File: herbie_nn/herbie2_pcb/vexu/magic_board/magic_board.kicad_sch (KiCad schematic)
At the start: 12 parts, among them J1 4P4C, J2 Conn_ARM_JTAG_SWD_10, U2 ATSAMD21G18A-A, U3 BD33FC0WEFJ, Y1 Crystal

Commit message: updated board
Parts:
- added LED1, LED2, PWR1: LED, LED_SMD:LED_1206_3216Metric, symbol Device:LED
- added R3: 10K, Resistor_SMD:R_1206_3216Metric, symbol Device:R
- added R4, R5, R6: 330, Resistor_SMD:R_1206_3216Metric, symbol Device:R
- added U4: ATSAMD51J19A-A, Package_QFP:TQFP-64_10x10mm_P0.5mm, symbol MCU_Microchip_SAMD:ATSAMD51J19A-A
- C1, C2: value C -> 15pF
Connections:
- net Vcc is gone; now on net +12V: J1.4
- net GND: now also BZ1.2 (-), C1.1, C2.1, D1.3 (common), J2.3 (GND), J2.5 (GND), U2.18 (GND), U2.35 (GND), U2.42 (GND), U2.5 (GNDANA), U3.3 (GND), U3.9 (GND), LED1.1 (K), LED2.1 (K), PWR1.1 (K), R3.2
- net RX_BRAIN: now reaches U1.1 (R)
- net RX_BRAIN: now also U2.10 (PA05)
- net DIR_BRAIN: now reaches U1.2 (RE/)
- net DIR_BRAIN: now also U1.3 (DE)
- net TX_BRAIN: now reaches U1.4 (D)
- net TX_BRAIN: now also U2.9 (PA04)
- net +3.3V: now reaches U1.8 (Vcc)
- net +3.3V: now also J2.1 (VTref), U2.17 (VDDIO), U2.36 (VDDIO), U2.44 (VDDIN), U3.1 (VO), R6.2
- net NRESET: now reaches J2.10 (~{RESET})
- net NRESET: now also U2.40 (~{RESET})
- net SWDIO: now reaches J2.2 (SWDIO/TMS)
- net SWDIO: now also U2.46 (PA31)
- net SWCLK: now reaches J2.4 (SWCLK/TCK)
- net SWCLK: now also U2.45 (PA30)
- net +12V: now reaches U3.5 (EN)
- net +12V: now also U3.8 (VCC), R3.1
- net at U2.37 (PB22): now also R4.2
- net at U2.38 (PB23): now also R5.2
- new net: LED2.2 (A), R5.1
- new net: U4.22 (GND), U4.33 (GND), U4.47 (GND), U4.54 (GND)
- new net: PWR1.2 (A), R6.1
- new net: LED1.2 (A), R4.1
- no-connect marks 0 -> 3
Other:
- moved on the sheet: C1, C2, R1, R2, U1, U3

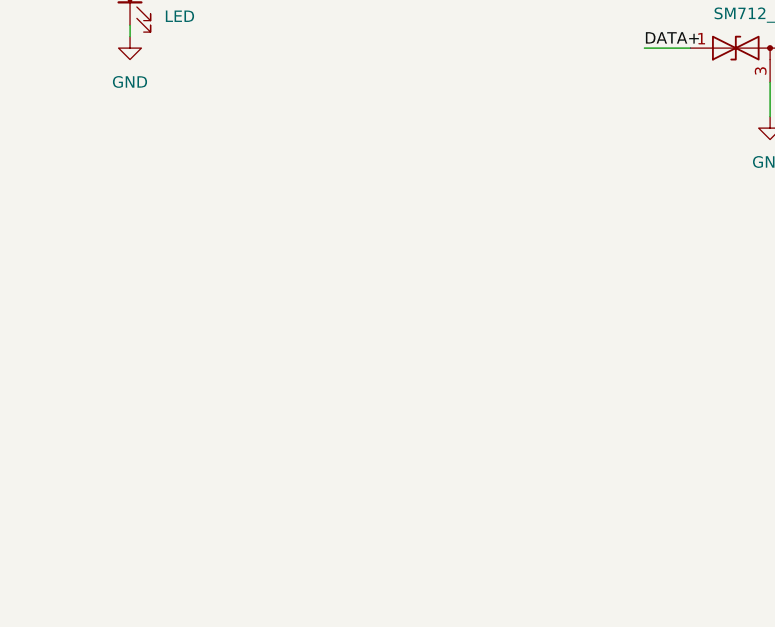
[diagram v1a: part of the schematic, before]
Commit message: added SAMD51 and encoder chips
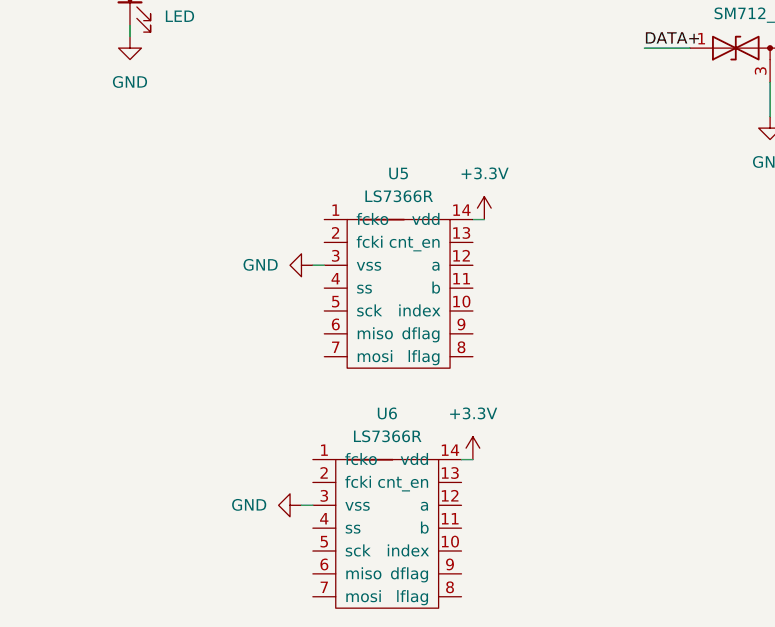
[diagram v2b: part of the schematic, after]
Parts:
- added U5, U6: LS7366R, Package_SO:SOIC-14_3.9x8.7mm_P1.27mm, symbol js:LS7366R
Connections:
- net +3.3V: now also U5.14 (vdd), U6.14 (vdd)
- net GND: now also U5.3 (vss), U6.3 (vss)

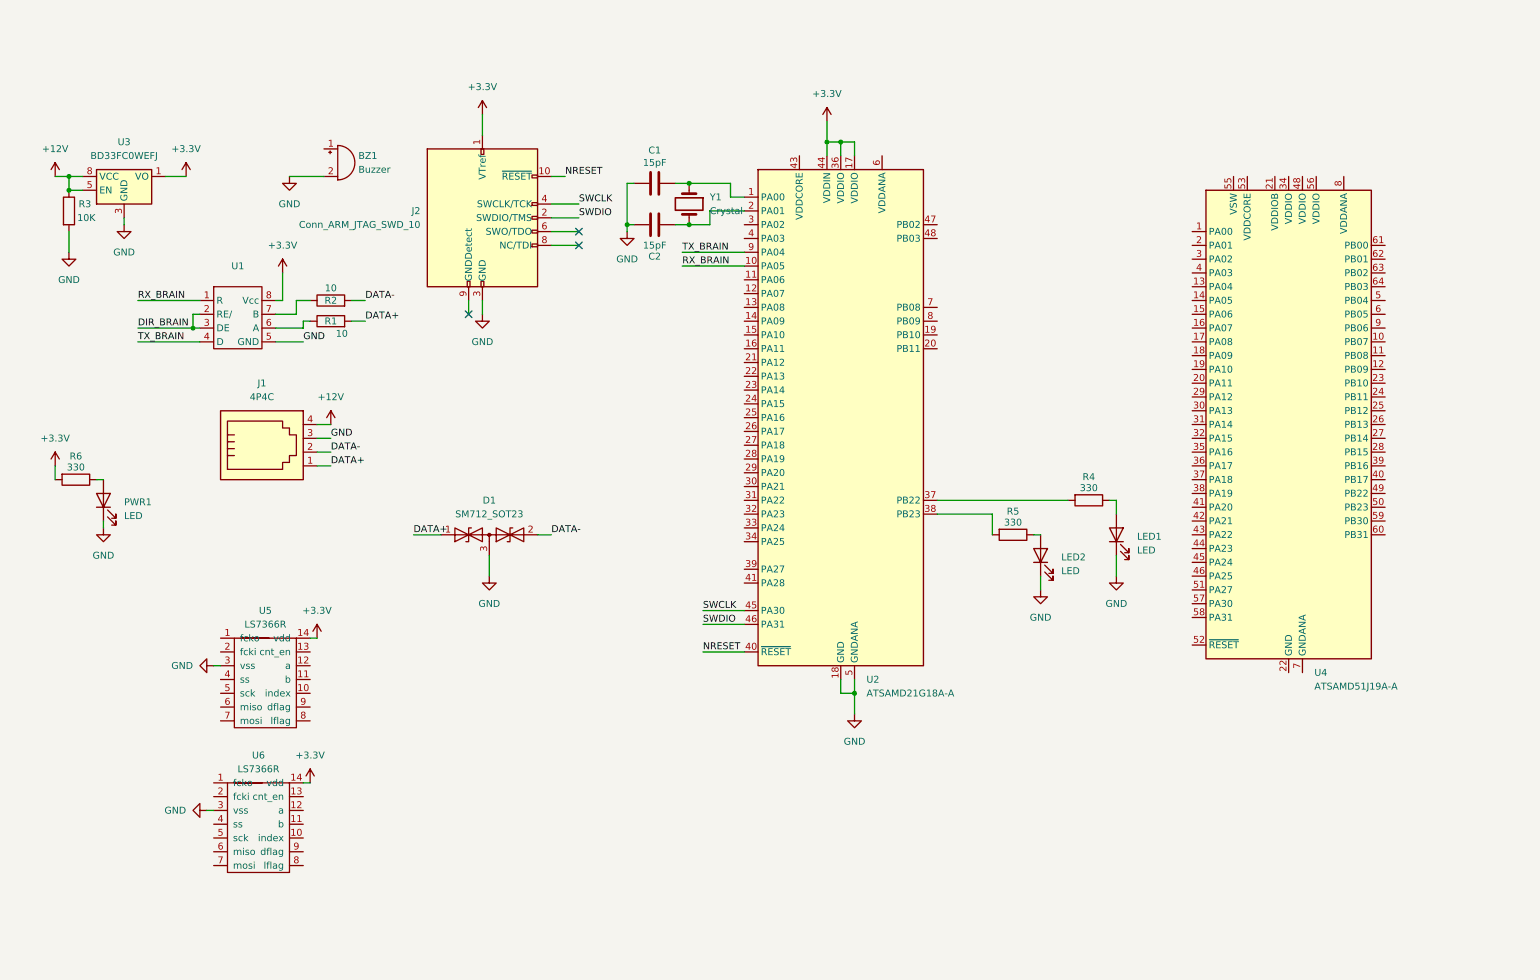
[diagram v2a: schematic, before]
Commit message: changed to SAMD51J19
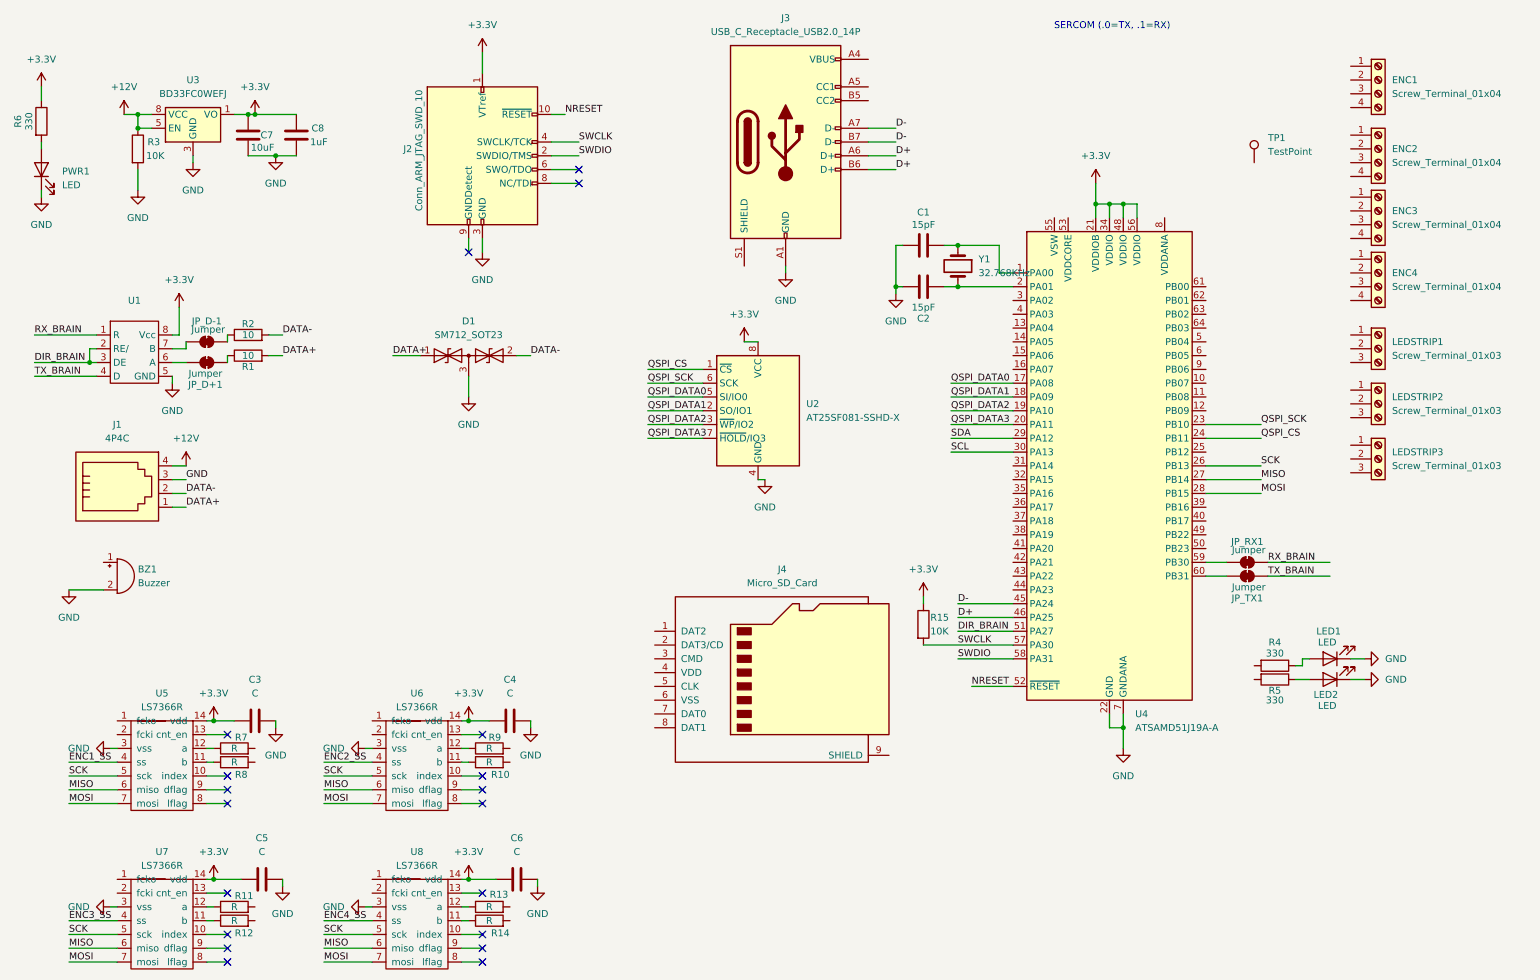
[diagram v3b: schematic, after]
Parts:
- removed U2: ATSAMD21G18A-A, Package_QFP:TQFP-48_7x7mm_P0.5mm, symbol MCU_Microchip_SAMD:ATSAMD21G18A-A
- added C3, C4, C5, C6: C, Capacitor_SMD:C_1206_3216Metric, symbol Device:C
- added C7: 10uF, Capacitor_SMD:C_1206_3216Metric, symbol Device:C
- added C8: 1uF, Capacitor_SMD:C_1206_3216Metric, symbol Device:C
- added ENC1, ENC2, ENC3, ENC4: Screw_Terminal_01x04, TerminalBlock_Phoenix:TerminalBlock_Phoenix_MPT-0,5-4-2.54_1x04_P2.54mm_Horizontal, symbol Connector:Screw_Terminal_01x04
- added J3: USB_C_Receptacle_USB2.0_14P, Connector_USB:USB_C_Receptacle_GCT_USB4085, symbol Connector:USB_C_Receptacle_USB2.0_14P
- added J4: Micro_SD_Card, Connector_Card:microSD_HC_Molex_104031-0811, symbol Connector:Micro_SD_Card
- added JP_D+1, JP_D-1, JP_RX1, JP_TX1: Jumper, Jumper:SolderJumper-2_P1.3mm_Open_Pad1.0x1.5mm, symbol Jumper:SolderJumper_2_Bridged
- added LEDSTRIP1, LEDSTRIP2, LEDSTRIP3: Screw_Terminal_01x03, TerminalBlock_Phoenix:TerminalBlock_Phoenix_MPT-0,5-3-2.54_1x03_P2.54mm_Horizontal, symbol Connector:Screw_Terminal_01x03
- added R10, R11, R12, R13, R14, R7, R8, R9: R, Resistor_SMD:R_1206_3216Metric, symbol Device:R
- added R15: 10K, Resistor_SMD:R_1206_3216Metric, symbol Device:R
- added TP1: TestPoint, TestPoint:TestPoint_Pad_D1.0mm, symbol Connector:TestPoint
- added U2: AT25SF081-SSHD-X, Package_SO:SOIC-8_3.9x4.9mm_P1.27mm, symbol Memory_Flash:AT25SF081-SSHD-X
- added U7, U8: LS7366R, Package_SO:SOIC-14_3.9x8.7mm_P1.27mm, symbol js:LS7366R
- Y1: value Crystal -> 32.768KHz
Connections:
- net +3.3V: now also R6.1, U4.21 (VDDIOB), U4.34 (VDDIO), U4.48 (VDDIO), U4.56 (VDDIO), C3.1, C4.1, C5.1, C6.1, C7.1, C8.1, R15.1, U2.8 (VCC), U7.14 (vdd), U8.14 (vdd); no longer R6.2
- net DIR_BRAIN: now also U4.51 (PA27)
- net GND: now also U4.22 (GND), U4.33 (GND), U4.47 (GND), U4.54 (GND), U4.7 (GNDANA), C3.2, C4.2, C5.2, C6.2, C7.2, C8.2, J3.A1 (GND), J3.A12 (GND), J3.B1 (GND), J3.B12 (GND), U2.4 (GND), U7.3 (vss), U8.3 (vss)
- net NRESET: now also U4.52 (~{RESET})
- net RX_BRAIN: now also JP_RX1.2 (B)
- net SWCLK: now also U4.57 (PA30), R15.2
- net SWDIO: now also U4.58 (PA31)
- net TX_BRAIN: now also JP_TX1.2 (B)
- net at R2.1: now also JP_D-1.2 (B); no longer U1.7 (B)
- net at U1.6 (A): now also JP_D+1.1 (A); no longer R1.1
- net at C1.2, Y1.1: now also U4.1 (PA00)
- net at C2.2, Y1.2: now also U4.2 (PA01)
- net at U6.11 (b): now also R10.1
- net at U6.12 (a): now also R9.1
- net ENC2_SS: now reaches U6.4 (ss)
- net SCK: now reaches U6.5 (sck)
- net SCK: now also U4.26 (PB13), U5.5 (sck), U7.5 (sck), U8.5 (sck)
- net MISO: now reaches U6.6 (miso)
- net MISO: now also U4.27 (PB14), U5.6 (miso), U7.6 (miso), U8.6 (miso)
- net MOSI: now reaches U6.7 (mosi)
- net MOSI: now also U4.28 (PB15), U5.7 (mosi), U7.7 (mosi), U8.7 (mosi)
- net QSPI_DATA0: now reaches U4.17 (PA08)
- net QSPI_DATA0: now also U2.5 (SI/IO0)
- net QSPI_DATA1: now reaches U4.18 (PA09)
- net QSPI_DATA1: now also U2.2 (SO/IO1)
- net QSPI_DATA2: now reaches U4.19 (PA10)
- net QSPI_DATA2: now also U2.3 (~{WP}/IO2)
- net QSPI_DATA3: now reaches U4.20 (PA11)
- net QSPI_DATA3: now also U2.7 (~{HOLD}/IO3)
- net QSPI_SCK: now reaches U4.23 (PB10)
- net QSPI_SCK: now also U2.6 (SCK)
- net QSPI_CS: now reaches U4.24 (PB11)
- net QSPI_CS: now also U2.1 (~{CS})
- net SDA: now reaches U4.29 (PA12)
- net SCL: now reaches U4.30 (PA13)
- net D-: now reaches U4.45 (PA24)
- net D-: now also J3.A7 (D-), J3.B7 (D-)
- net D+: now reaches U4.46 (PA25)
- net D+: now also J3.A6 (D+), J3.B6 (D+)
- net at U4.59 (PB30): now also JP_RX1.1 (A)
- net at U4.60 (PB31): now also JP_TX1.1 (A)
- net at PWR1.2 (A): now also R6.2; no longer R6.1
- net at U5.11 (b): now also R8.1
- net at U5.12 (a): now also R7.1
- net ENC1_SS: now reaches U5.4 (ss)
- new net: R12.1, U7.11 (b)
- new net: R11.1, U7.12 (a)
- new net: R13.1, U8.12 (a)
- new net: R14.1, U8.11 (b)
- new net: JP_D-1.1 (A), U1.7 (B)
- new net: J3.A4 (VBUS), J3.A9 (VBUS), J3.B4 (VBUS), J3.B9 (VBUS)
- new net: JP_D+1.2 (B), R1.1
- new net ENC3_SS: U7.4 (ss)
- new net ENC4_SS: U8.4 (ss)
- no-connect marks 3 -> 19
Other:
- note added: "SERCOM (.0=TX, .1=RX)"
- moved on the sheet: BZ1, C1, C2, D1, J1, J2, LED1, LED2, PWR1, R1, R2, R3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

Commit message: updated board
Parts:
- removed J4: Micro_SD_Card, Connector_Card:microSD_HC_Molex_104031-0811, symbol Connector:Micro_SD_Card
- removed R8: R, Resistor_SMD:R_1206_3216Metric, symbol Device:R
- added C10, C9: C, Capacitor_SMD:C_1206_3216Metric, symbol Device:C
- added H1, H2, H3, H4: MountingHole, MountingHole:MountingHole_3.2mm_M3_DIN965, symbol Mechanical:MountingHole
- added J4, J5: Conn_01x04_Pin, Connector_PinHeader_2.54mm:PinHeader_1x04_P2.54mm_Vertical, symbol Connector:Conn_01x04_Pin
- added R16, R17: R, Resistor_SMD:R_1206_3216Metric, symbol Device:R
- added U10, U9: SN74LVC245APW, Package_SO:TSSOP-20_4.4x6.5mm_P0.65mm, symbol Logic_LevelTranslator:SN74LVC245APW
- added U11: 74HC14, Package_SO:TSSOP-14_4.4x5mm_P0.65mm, symbol 74xx:74HC14
- added Y2: 20MHz, Crystal:Crystal_SMD_2012-2Pin_2.0x1.2mm_HandSoldering, symbol Device:Crystal
- BZ1: footprint Buzzer_Beeper:Buzzer_12x9.5RM7.6 -> Buzzer_Beeper:Buzzer_TDK_PS1240P02BT_D12.2mm_H6.5mm
- R7: value R -> 1M
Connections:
- net +12V: now also LEDSTRIP1.3 (Pin_3), LEDSTRIP2.3 (Pin_3), LEDSTRIP3.3 (Pin_3)
- net +3.3V: now also U10.1 (DIR), U10.20 (VCC), U9.20 (VCC)
- net ENC1_SS: now also U4.5 (PB04)
- net ENC2_SS: now also U4.6 (PB05)
- net ENC3_SS: now also U4.9 (PB06)
- net ENC4_SS: now also U4.10 (PB07)
- net GND: now also LEDSTRIP1.1 (Pin_1), LEDSTRIP2.1 (Pin_1), LEDSTRIP3.1 (Pin_1), C10.1, C9.1, U10.10 (GND), U10.19 (~{OE}), U9.10 (GND)
- net A4_IN: now reaches ENC4.2 (Pin_2)
- net A4_IN: now also R16.1
- net B4_IN: now reaches ENC4.3 (Pin_3)
- net B4_IN: now also R17.1
- net B2_IN: now reaches R12.1
- net B2_IN: now also ENC2.3 (Pin_3); no longer U7.11 (b)
- net at R12.2: now also U9.5 (A4)
- net A2_IN: now reaches R11.1
- net A2_IN: now also ENC2.2 (Pin_2); no longer U7.12 (a)
- net at R11.2: now also U9.4 (A3)
- net A3_IN: now reaches R13.1
- net A3_IN: now also ENC3.2 (Pin_2); no longer U8.12 (a)
- net at R13.2: now also U10.6 (A5)
- net B3_IN: now reaches R14.1
- net B3_IN: now also ENC3.3 (Pin_3); no longer U8.11 (b)
- net OUT_CLK: now reaches U8.2 (fcki)
- net OUT_CLK: now also U6.2 (fcki), U7.2 (fcki), U11.2
- net at R14.2: now also U10.7 (A6)
- net A1_IN: now reaches ENC1.2 (Pin_2)
- net A1_IN: now also R9.1
- net B1_IN: now reaches ENC1.3 (Pin_3)
- net B1_IN: now also R10.1
- net B2: now reaches U6.11 (b)
- net B2: now also U9.15 (B4); no longer R10.1
- net A2: now reaches U6.12 (a)
- net A2: now also U9.16 (B3); no longer R9.1
- net BUZ_PIN: now reaches U4.11 (PB08)
- net BUZ_PIN: now also BZ1.1 (+)
- net SERCOM0.0: now reaches U4.13 (PA04)
- net SERCOM0.1: now reaches U4.14 (PA05)
- net SERCOM0.2: now reaches U4.15 (PA06)
- net SERCOM0.3: now reaches U4.16 (PA07)
- net DAC_OUT0: now reaches U4.3 (PA02)
- net SERCOM1.0: now reaches U4.35 (PA16)
- net SERCOM1.1: now reaches U4.36 (PA17)
- net SERCOM1.2: now reaches U4.37 (PA18)
- net SERCOM1.3: now reaches U4.38 (PA19)
- net LED_SIG3: now reaches U4.62 (PB01)
- net LED_SIG3: now also LEDSTRIP3.2 (Pin_2)
- net LED_SIG2: now reaches U4.63 (PB02)
- net LED_SIG2: now also LEDSTRIP2.2 (Pin_2)
- net LED_SIG1: now reaches U4.64 (PB03)
- net LED_SIG1: now also LEDSTRIP1.2 (Pin_2)
- net at R10.2: now also U9.3 (A2)
- net at R9.2: now also U9.2 (A1)
- net B1: now reaches U5.11 (b)
- net B1: now also U9.17 (B2)
- net at R7.1: now also U5.2 (fcki), C9.2, Y2.1; no longer U5.12 (a)
- net EN_CLK: now reaches R7.2
- net EN_CLK: now also U5.1 (fcko), C10.2, U11.1, Y2.2
- new net: R17.2, U10.9 (A8)
- new net: R16.2, U10.8 (A7)
- new net A1: U5.12 (a), U9.18 (B1)
- new net A3: U10.14 (B5), U7.12 (a)
- new net A4: U10.12 (B7), U8.12 (a)
- new net B3: U10.13 (B6), U7.11 (b)
- new net B4: U10.11 (B8), U8.11 (b)
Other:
- note added: "Encoders using SERCOM4"
- note added: "LED_SIG3 = using Timer 7 LED_SIG1/2 = using Timer 6 Buzzer using Timer 4"
- note added: "Using SERCOM5 for Vex Brain"
- moved on the sheet: C3, C4, C5, C6, D1, J2, LEDSTRIP1, LEDSTRIP2, LEDSTRIP3, U5, U6, U7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

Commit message: change regulator
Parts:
- removed U3: BD33FC0WEFJ, Package_SO:HTSOP-8-1EP_3.9x4.9mm_P1.27mm_EP2.4x3.2mm, symbol Regulator_Linear:BD33FC0WEFJ
- added C11, C12, C13, C14: C, Capacitor_SMD:C_1206_3216Metric, symbol Device:C
- added D2, D3: MBR1020VL, Diode_SMD:D_SOD-123F, symbol Diode:MBR1020VL
- added JP1, JP2, JP3, JP4: SolderJumper_3_Open, Jumper:SolderJumper-3_P1.3mm_Open_Pad1.0x1.5mm, symbol Jumper:SolderJumper_3_Open
- added R18, R19, R8: R, Resistor_SMD:R_1206_3216Metric, symbol Device:R
- added U12: AMS1117-5.0, Package_TO_SOT_SMD:SOT-223-3_TabPin2, symbol Regulator_Linear:AMS1117-5.0
- added U13: AP2112K-3.3, Package_TO_SOT_SMD:SOT-23-5, symbol Regulator_Linear:AP2112K-3.3
- added U3: LM386, Package_SO:SOIC-8-1EP_3.9x4.9mm_P1.27mm_EP2.29x3mm, symbol Amplifier_Audio:LM386
- Y2: value 20MHz -> 8MHz
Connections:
- net +12V: now also U12.3 (VI); no longer R3.1
- net +3.3V: now also U9.1 (DIR), JP1.3 (B), JP2.3 (B), JP3.3 (B), JP4.3 (B), U13.5 (VOUT)
- net DAC_OUT0: now also C14.1
- net GND: now also U9.19 (~{OE}), R19.2, R8.2, U12.1 (GND), U13.2 (GND), U3.2 (-), U3.4 (GND)
- net at ENC4.4 (Pin_4): now also JP4.2 (C)
- net at ENC1.4 (Pin_4): now also JP1.2 (C)
- net at J3.A4 (VBUS), J3.A9 (VBUS), J3.B4 (VBUS)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: now also D2.2 (A)
- net at ENC2.4 (Pin_4): now also JP2.2 (C)
- net at ENC3.4 (Pin_4): now also JP3.2 (C)
- new net: C14.2, R18.1
- new net: R18.2, R19.1, U3.3 (+)
- new net: C12.2, R8.1
- new net: D3.2 (A), U12.2 (VO)
- new net: C11.1, C12.1, U3.5
- new net: C13.1, U3.1 (GAIN)
- new net: C13.2, U3.8 (GAIN)
- new net +5V: D2.1 (K), D3.1 (K), JP1.1 (A), JP2.1 (A), JP3.1 (A), JP4.1 (A), R3.1, U13.1 (VIN), U13.3 (EN), U3.6 (V+)
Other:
- moved on the sheet: BZ1, C1, C10, C2, C3, C4, C5, C6, C7, C8, C9, D1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

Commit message: updated encoder chip
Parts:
- removed C4, C5: C, Capacitor_SMD:C_1206_3216Metric, symbol Device:C
- removed R10, R11, R12, R13, R14, R16, R17, R9: R, Resistor_SMD:R_1206_3216Metric, symbol Device:R
- removed U10, U9: SN74LVC245APW, Package_SO:TSSOP-20_4.4x6.5mm_P0.65mm, symbol Logic_LevelTranslator:SN74LVC245APW
- removed U11: 74HC14, Package_SO:TSSOP-14_4.4x5mm_P0.65mm, symbol 74xx:74HC14
- added R20, R21, R22, R23, R24, R25, R26, R27: R, Resistor_SMD:R_1206_3216Metric, symbol Device:R
- added U11, U15: 74LVC125, Package_SO:TSSOP-14_4.4x5mm_P0.65mm, symbol 74xx:74LVC125
- added U14: 74LVC2G14, Package_SO:TSOP-6_1.65x3.05mm_P0.95mm, symbol 74xGxx:74LVC2G14
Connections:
- net +3.3V: now also U11.14 (VCC), U14.5 (VCC), U15.14 (VCC)
- net A1: now also U11.3
- net A1_IN: now also R20.1
- net A2: now also U11.8
- net A2_IN: now also R22.1
- net A3: now also U15.3
- net A3_IN: now also R24.1
- net A4: now also U15.8
- net A4_IN: now also R26.1
- net B1: now also U11.6
- net B1_IN: now also R21.1
- net B2: now also U11.11
- net B2_IN: now also R23.1
- net B3: now also U15.6
- net B3_IN: now also R25.1
- net B4: now also U15.11
- net B4_IN: now also R27.1
- net EN_CLK: now also U14.1
- net GND: now also U11.1, U11.10, U11.13, U11.4, U11.7 (GND), U14.2 (GND), U15.1, U15.10, U15.13, U15.4, U15.7 (GND)
- net OUT_CLK: now also U14.6
- new net: R22.2, U11.9
- new net: R20.2, U11.2
- new net: R26.2, U15.9
- new net: R24.2, U15.2
- new net: R25.2, U15.5
- new net: R27.2, U15.12
- new net: R21.2, U11.5
- new net: R23.2, U11.12
- no-connect marks 19 -> 21
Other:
- moved on the sheet: BZ1, C1, C10, C11, C12, C13, C14, C2, C3, C6, C7, C8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
